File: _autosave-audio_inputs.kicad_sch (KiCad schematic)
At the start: 8 parts, among them IC1 WM8804GEDS_V, J2 AFBR-2624Z, Y1 12.288 MHz

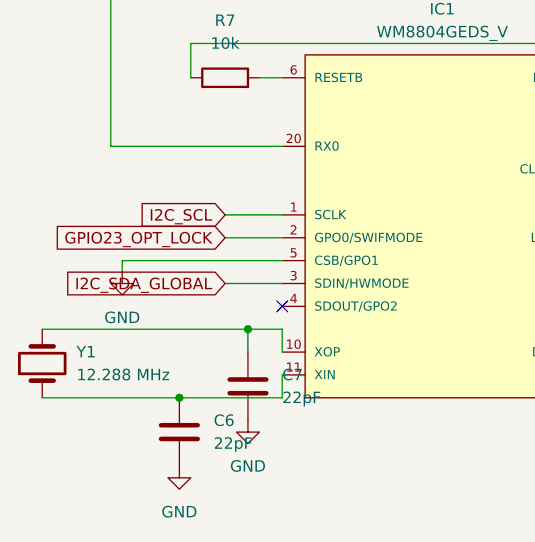
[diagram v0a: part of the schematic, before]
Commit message: Some cleanup of schematic symbols etc.
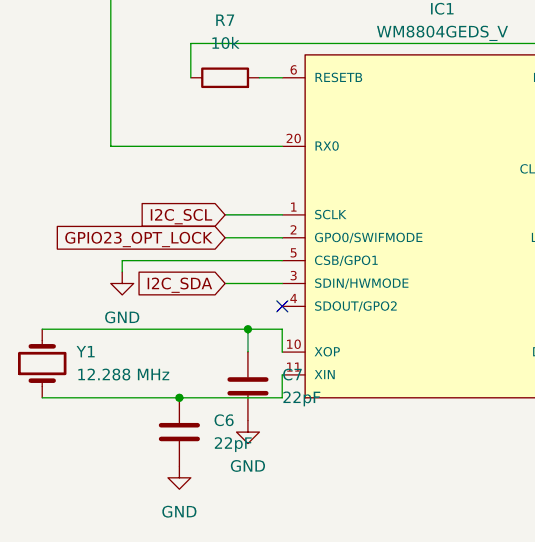
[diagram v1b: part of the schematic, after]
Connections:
- net I2C_SDA_GLOBAL renamed I2C_SDA
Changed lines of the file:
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@@
 		)
 	)
-	(global_label "I2C_SDA_GLOBAL"
+	(global_label "I2C_SDA"
 		(shape input)
 		(at 71.12 76.2 180)
@@
 		)
 		(property "Intersheetrefs" "${INTERSHEET_REFS}"
-			(at 52.4368 76.2 0)
+			(at 60.4197 76.2 0)
 			(effects
 				(font
